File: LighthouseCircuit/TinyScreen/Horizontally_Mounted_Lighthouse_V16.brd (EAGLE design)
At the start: 25.4 x 8.9 mm, 23 parts

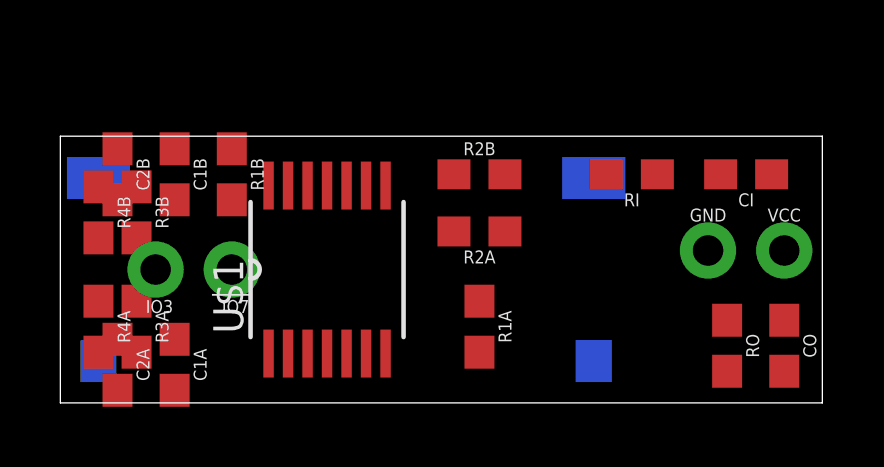
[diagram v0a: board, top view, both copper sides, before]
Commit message: Working on initial demo of multiple Zippies in coordination.
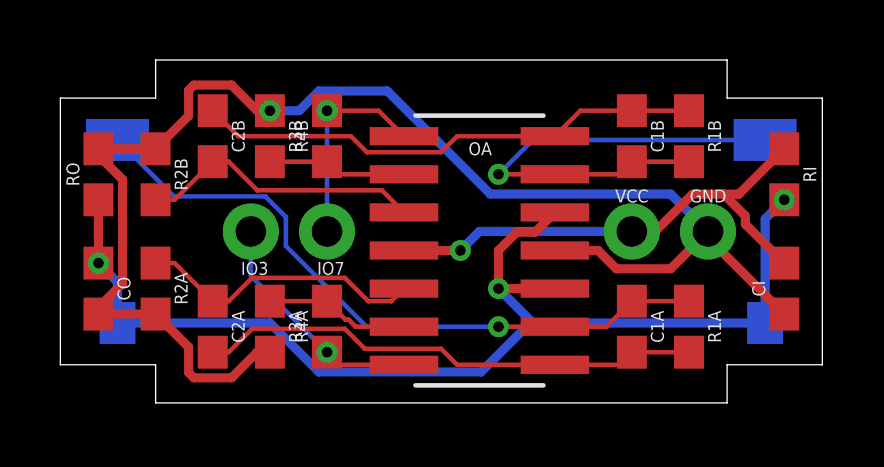
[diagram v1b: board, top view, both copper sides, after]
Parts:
- removed U$1: TLV2464IPW, ZippyComponentLibrary:PW14
- added OA: TLV2464IDM, ZippyComponentLibrary:D14-M
- C1A, C1B: value 5pF -> 2.2pF
- R1A, R1B: value 100k -> 27k
- R2A, R2B: value 18k -> 100k
- moved CO 22.9 mm to (1.27, 3.81)
- moved RO 21.7 mm to (1.27, 7.62), turned to 270 degrees
- moved C1A 15.3 mm to (19.1, 2.54)
- moved C1B 15.3 mm to (19.1, 8.89)
- moved R1B 15.3 mm to (21.0, 8.89)
- moved R2A 11.0 mm to (3.17, 3.81), turned to 270 degrees
- moved R2B 10.8 mm to (3.17, 7.62), turned to 90 degrees
- moved R4B 8.03 mm to (8.89, 8.89), turned to 90 degrees
- moved R4A 7.62 mm to (8.89, 2.54), turned to 270 degrees
- moved R1A 6.98 mm to (21.0, 2.54)
- moved D2 5.85 mm to (23.5, 5.71)
- moved R3B 5.12 mm to (6.99, 8.89)
- moved VCC 5.12 mm to (19.1, 5.71)
- moved RI 5.08 mm to (24.1, 7.62), turned to 90 degrees
- moved R3A 4.45 mm to (6.99, 2.54)
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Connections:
- removed net D2OA2N: R3A.1, R4A.1, U$1.5
- new net N$1: OA.6, R3A.1, R4A.1
- net D1IN: now also OA.13; no longer U$1.13
- net D1OA2P: now also OA.3; no longer U$1.2
- net D1OAOUT1: now also OA.14; no longer U$1.14
- net D2IN: now also OA.9; no longer U$1.9
- net D2OA1OUT: now also OA.8; no longer U$1.8
- net D2OA2P: now also OA.5; no longer U$1.6
- net GND: now also OA.11, R2A.2, R2B.2, R3A.2, R3B.2; no longer U$1.11
- net IO3: now also OA.7; no longer U$1.7
- net IO7: now also OA.1; no longer U$1.1
- net LVCC: now also OA.10, OA.12; no longer R2A.2, R2B.2, R3A.2, R3B.2, U$1.10, U$1.12
- net N$11: now also OA.2; no longer U$1.3
- net VCC: now also OA.4; no longer U$1.4
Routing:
- net GND: track 0.00 -> 47.6 mm, vias 0 -> 1
- net LVCC: track 0.00 -> 38.9 mm, vias 0 -> 3
- net D2IN: track 0.00 -> 22.5 mm, vias 0 -> 1
- net VCC: track 0.00 -> 17.2 mm, vias 0 -> 1
- net D1OAOUT1: track 0.00 -> 17.0 mm
- net D2OA1OUT: track 0.00 -> 16.9 mm
- net D1IN: track 0.00 -> 15.9 mm, vias 0 -> 1
- net D2OA2P: track 0.00 -> 9.63 mm
- net D1OA2P: track 0.00 -> 9.51 mm
- net IO3: track 0.00 -> 7.82 mm, vias 0 -> 1
- net IO7: track 0.00 -> 6.94 mm, vias 0 -> 1
- net N$1: track 0.00 -> 4.82 mm
- net N$11: track 0.00 -> 4.64 mm
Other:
- board size 25.4 x 8.9 mm -> 25.4 x 11.4 mm
- board text added: "v1.6"
